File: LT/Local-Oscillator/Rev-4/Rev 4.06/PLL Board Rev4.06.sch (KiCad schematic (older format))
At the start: 69 parts, among them J1 Conn_01x02_Male, J13 Conn_01x02_Male, J14 Conn_01x02_Male, J15 Conn_01x02_Male, J16 Conn_01x02_Male, J17 Conn_01x02_Male, J18 Conn_Coaxial, J2 Conn_Coaxial, J20 Conn_01x02_Male, J3 Conn_Coaxial, J4 Conn_01x04_Male, J5 Conn_01x02_Male, J7 Conn_01x02_Male, J8 Conn_01x02_Male, Q1 2N5486 JFET, Q2 2N5486 JFET, U1 LMX231X, U2 L7808

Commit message: Finished PLL Revisions on KiCad
The KiCad files for the PLL have been uploaded to github and the integration to the "Real Resistor" symbol has begun
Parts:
- removed R1, R3, R4: 18, Resistor_SMD:R_0805_2012Metric_Pad1.15x1.40mm_HandSolder, symbol Device:R
- removed R10: 100k, Resistor_SMD:R_0805_2012Metric_Pad1.15x1.40mm_HandSolder, symbol Device:R
- removed R11, R12, R6, R9: 1k, Resistor_SMD:R_0805_2012Metric_Pad1.15x1.40mm_HandSolder, symbol Device:R
- removed R2: 10k, Resistor_SMD:R_0805_2012Metric_Pad1.15x1.40mm_HandSolder, symbol Device:R
- removed R5: R, Resistor_SMD:R_0805_2012Metric_Pad1.15x1.40mm_HandSolder, symbol Device:R
- removed R7: 62k, Resistor_SMD:R_0805_2012Metric_Pad1.15x1.40mm_HandSolder, symbol Device:R
- removed R8: 1ohm, Resistor_SMD:R_0805_2012Metric_Pad1.15x1.40mm_HandSolder, symbol Device:R
- added R1, R3, R4: 18, Resistor_SMD:R_0805_2012Metric_Pad1.15x1.40mm_HandSolder, symbol PLL-Board-Rev4.06-rescue:R-Device-Complete-PLL-Board-Rev4-rescue-PLL-Board-Rev4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
- added R10: 100k, Resistor_SMD:R_0805_2012Metric_Pad1.15x1.40mm_HandSolder, symbol PLL-Board-Rev4.06-rescue:R-Device-Complete-PLL-Board-Rev4-rescue-PLL-Board-Rev4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
- added R11, R12, R6, R9: 1k, Resistor_SMD:R_0805_2012Metric_Pad1.15x1.40mm_HandSolder, symbol PLL-Board-Rev4.06-rescue:R-Device-Complete-PLL-Board-Rev4-rescue-PLL-Board-Rev4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
- added R2: 10k, Resistor_SMD:R_0805_2012Metric_Pad1.15x1.40mm_HandSolder, symbol PLL-Board-Rev4.06-rescue:R-Device-Complete-PLL-Board-Rev4-rescue-PLL-Board-Rev4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
- added R5: R, Resistor_SMD:R_0805_2012Metric_Pad1.15x1.40mm_HandSolder, symbol PLL-Board-Rev4.06-rescue:R-Device-Complete-PLL-Board-Rev4-rescue-PLL-Board-Rev4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
- added R7: 62k, Resistor_SMD:R_0805_2012Metric_Pad1.15x1.40mm_HandSolder, symbol PLL-Board-Rev4.06-rescue:R-Device-Complete-PLL-Board-Rev4-rescue-PLL-Board-Rev4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
- added R8: 1 Ohm, Resistor_SMD:R_0805_2012Metric_Pad1.15x1.40mm_HandSolder, symbol PLL-Board-Rev4.06-rescue:R-Device-Complete-PLL-Board-Rev4-rescue-PLL-Board-Rev4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
- C15: value 47pF -> 18pF
- C16: value 100pF -> 47pF
- C19: value TZB4Z100BA10R00 -> SGC35060
- D3, D4: value 1SV232 -> BB181
- R13, R14: symbol PLL-Board-Rev4.01-rescue:R-Device-Complete-PLL-Board-Rev4-rescue -> PLL-Board-Rev4.06-rescue:R-Device-Complete-PLL-Board-Rev4-rescue-PLL-Board-Rev4.01-rescue-PLL-Board-Rev4.02-rescue-PLL-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
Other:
- note added: "Rev4.06: Varactors changed from an unknown component to the BB181"

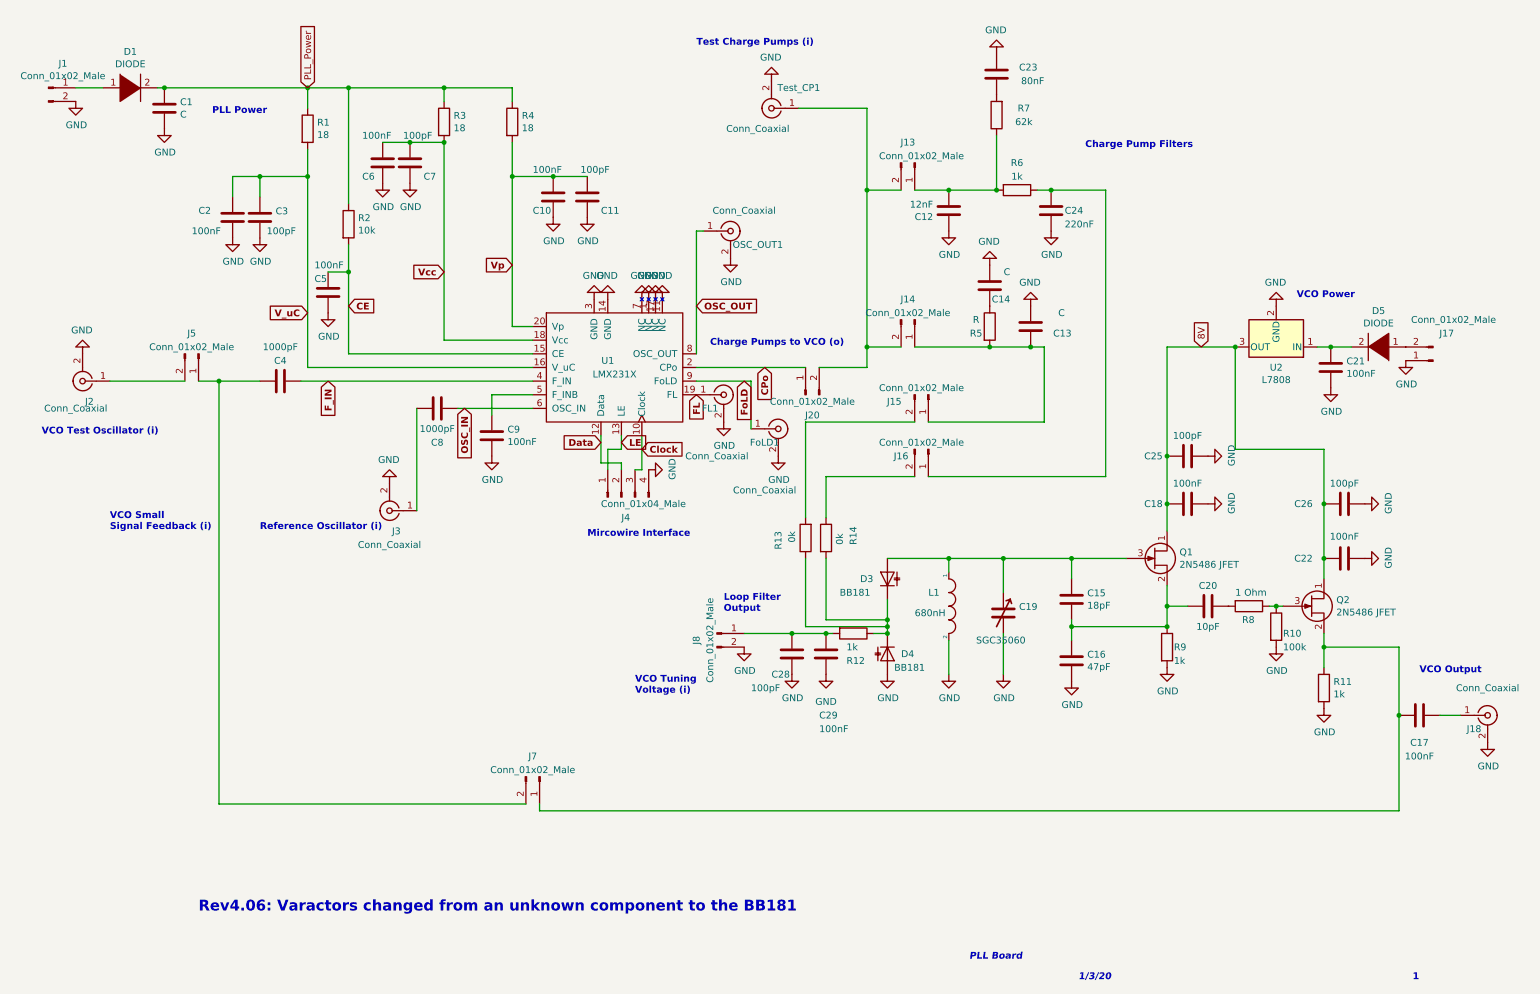
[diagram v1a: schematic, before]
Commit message: Finished PLL Resistor Symbols
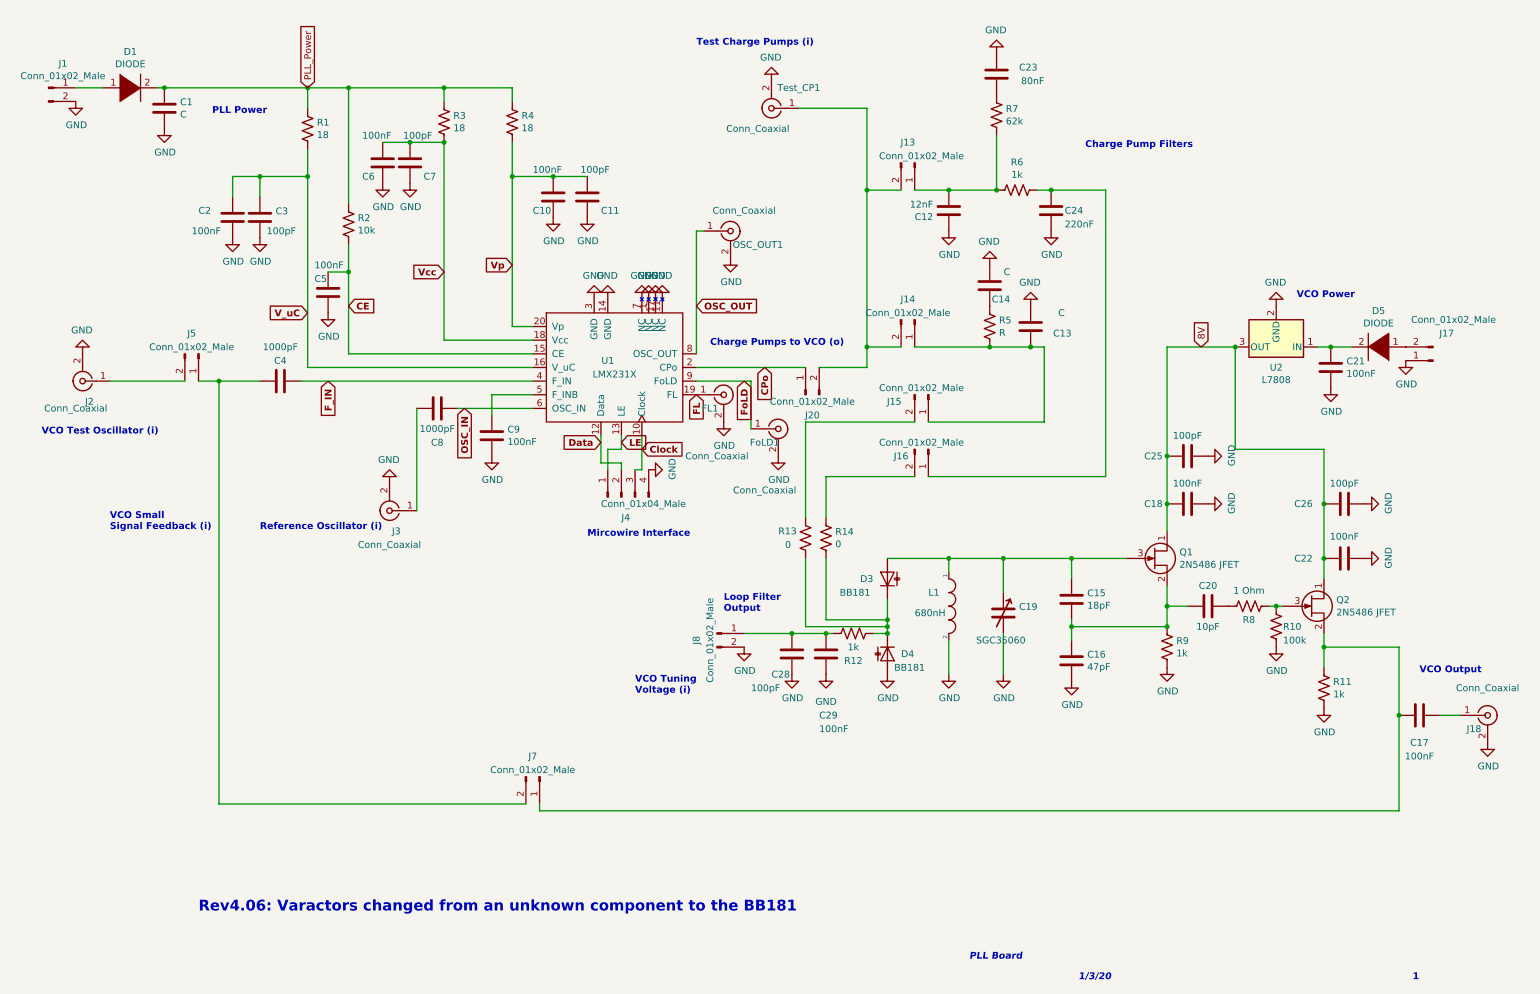
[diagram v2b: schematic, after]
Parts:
- removed R1, R3, R4: 18, Resistor_SMD:R_0805_2012Metric_Pad1.15x1.40mm_HandSolder, symbol PLL-Board-Rev4.06-rescue:R-Device-Complete-PLL-Board-Rev4-rescue-PLL-Board-Rev4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
- removed R10: 100k, Resistor_SMD:R_0805_2012Metric_Pad1.15x1.40mm_HandSolder, symbol PLL-Board-Rev4.06-rescue:R-Device-Complete-PLL-Board-Rev4-rescue-PLL-Board-Rev4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
- removed R11, R12, R6, R9: 1k, Resistor_SMD:R_0805_2012Metric_Pad1.15x1.40mm_HandSolder, symbol PLL-Board-Rev4.06-rescue:R-Device-Complete-PLL-Board-Rev4-rescue-PLL-Board-Rev4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
- removed R13, R14: 0k, Resistor_SMD:R_0805_2012Metric_Pad1.15x1.40mm_HandSolder, symbol PLL-Board-Rev4.06-rescue:R-Device-Complete-PLL-Board-Rev4-rescue-PLL-Board-Rev4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
- removed R2: 10k, Resistor_SMD:R_0805_2012Metric_Pad1.15x1.40mm_HandSolder, symbol PLL-Board-Rev4.06-rescue:R-Device-Complete-PLL-Board-Rev4-rescue-PLL-Board-Rev4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
- removed R5: R, Resistor_SMD:R_0805_2012Metric_Pad1.15x1.40mm_HandSolder, symbol PLL-Board-Rev4.06-rescue:R-Device-Complete-PLL-Board-Rev4-rescue-PLL-Board-Rev4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
- removed R7: 62k, Resistor_SMD:R_0805_2012Metric_Pad1.15x1.40mm_HandSolder, symbol PLL-Board-Rev4.06-rescue:R-Device-Complete-PLL-Board-Rev4-rescue-PLL-Board-Rev4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
- removed R8: 1 Ohm, Resistor_SMD:R_0805_2012Metric_Pad1.15x1.40mm_HandSolder, symbol PLL-Board-Rev4.06-rescue:R-Device-Complete-PLL-Board-Rev4-rescue-PLL-Board-Rev4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
- added R1, R3, R4: 18, Resistor_SMD:R_0805_2012Metric_Pad1.15x1.40mm_HandSolder, symbol Device:R_US
- added R10: 100k, Resistor_SMD:R_0805_2012Metric_Pad1.15x1.40mm_HandSolder, symbol Device:R_US
- added R11, R12, R6, R9: 1k, Resistor_SMD:R_0805_2012Metric_Pad1.15x1.40mm_HandSolder, symbol Device:R_US
- added R13, R14: 0, Resistor_SMD:R_0805_2012Metric_Pad1.15x1.40mm_HandSolder, symbol Device:R_US
- added R2: 10k, Resistor_SMD:R_0805_2012Metric_Pad1.15x1.40mm_HandSolder, symbol Device:R_US
- added R5: R, Resistor_SMD:R_0805_2012Metric_Pad1.15x1.40mm_HandSolder, symbol Device:R_US
- added R7: 62k, Resistor_SMD:R_0805_2012Metric_Pad1.15x1.40mm_HandSolder, symbol Device:R_US
- added R8: 1 Ohm, Resistor_SMD:R_0805_2012Metric_Pad1.15x1.40mm_HandSolder, symbol Device:R_US
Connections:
- net CE: now also R2.2
- net GND: now also R10.2, R11.2, R9.2
- net PLL_Power: now also R1.1, R2.1, R3.1, R4.1
- net V_uC: now also R1.2
- net Vcc: now also R3.2
- net Vp: now also R4.2
- net at C15.1, C16.2, C20.1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: now also R9.1
- net at D3.1 (K), D4.1 (K): now also R12.1, R13.2, R14.2
- net at C20.2: now also R8.2
- net at Q2.3 (G): now also R10.1, R8.1
- net at C17.1, J7.1 (Pin_1), Q2.2 (S): now also R11.1
- net at C13.1, J14.1 (Pin_1), J15.1 (Pin_1): now also R5.2
- net at C12.2, J13.1 (Pin_1): now also R6.2, R7.2
- net at C24.1, J16.1 (Pin_1): now also R6.1
- net at J15.2 (Pin_2): now also R13.1
- net at C28.2, C29.2, J8.1 (Pin_1): now also R12.2
- net at C14.1: now also R5.1
- net at J16.2 (Pin_2): now also R14.1
- net at C23.1: now also R7.1
